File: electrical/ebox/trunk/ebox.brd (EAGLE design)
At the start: 127 x 101.6 mm, 159 parts, among them IC1 MAX3221CUE, IC10 SN74LVC1G125, IC11 MAX3221CUE, IC12 INA170, IC13 SN74LVC1G125, IC14 SN74LVC1G125, IC15 MAX3221CUE, IC16 MCP170333MB, IC17 SN74LVC1G125, IC18 SN74LVC1G125, IC19 74ALS04D, IC2 LT3652, IC3 XMEGA128A1, IC4 LT1161, IC5 SN74LVC1G125, IC6 SN74LVC1G125, IC7 MAX3221CUE, IC8 INA170, IC9 SN74LVC1G125, Q1 FDD4141TO252, U1 BLUETOOTH-RN42, U2 D2523T_, X1 7381-3PG-300, X10 DEANS-MALE, X11 B4B-ZR, X12 DEANS-MALE, X13 B4B-ZR, X14 22-23-2021, X15 DEANS-FEMALE, X16 DEANS-FEMALE, X17 USB_A, X2 7381-3PG-300, X3 7381-2PG-300, X4 17984-7PG-300, X5 17984-7PG-300, X6 17984-7PG-300, X7 17984-7PG-300, X8 22-23-2031, X9 22-23-2031

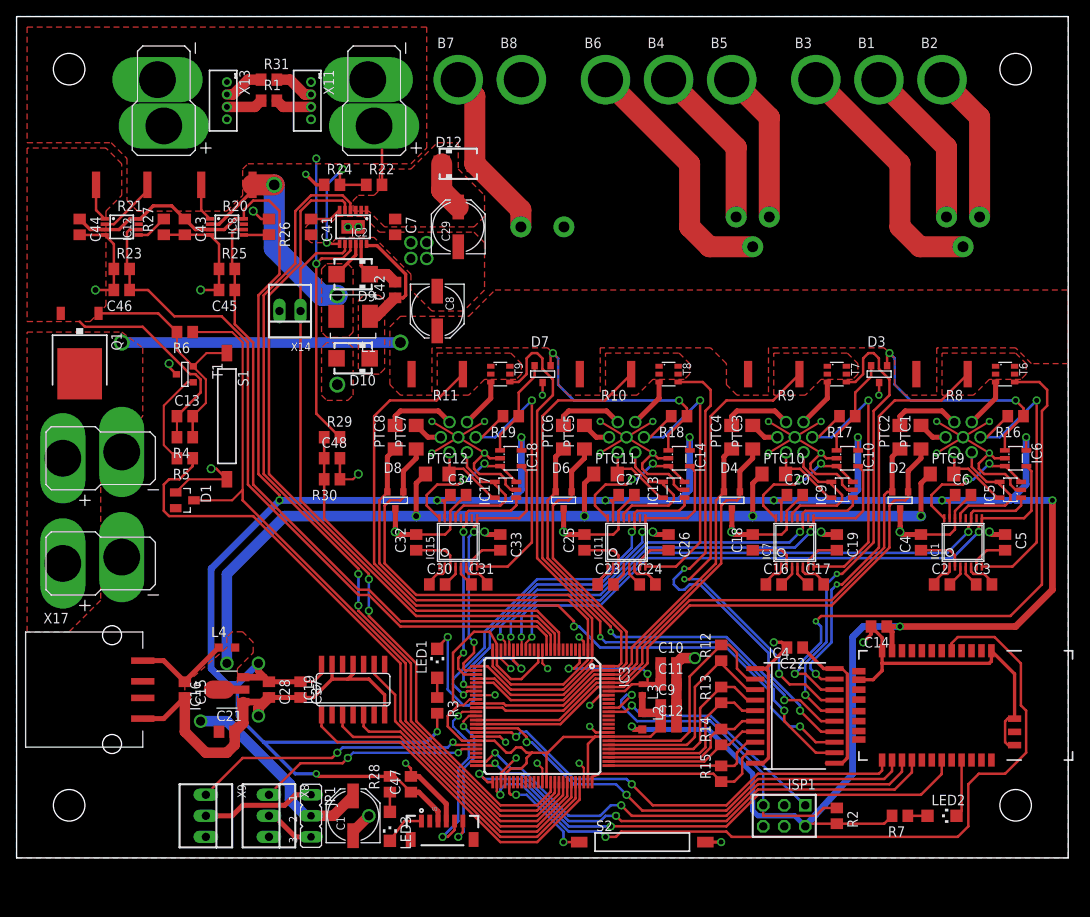
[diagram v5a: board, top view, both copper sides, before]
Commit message: Added water sensor connection.
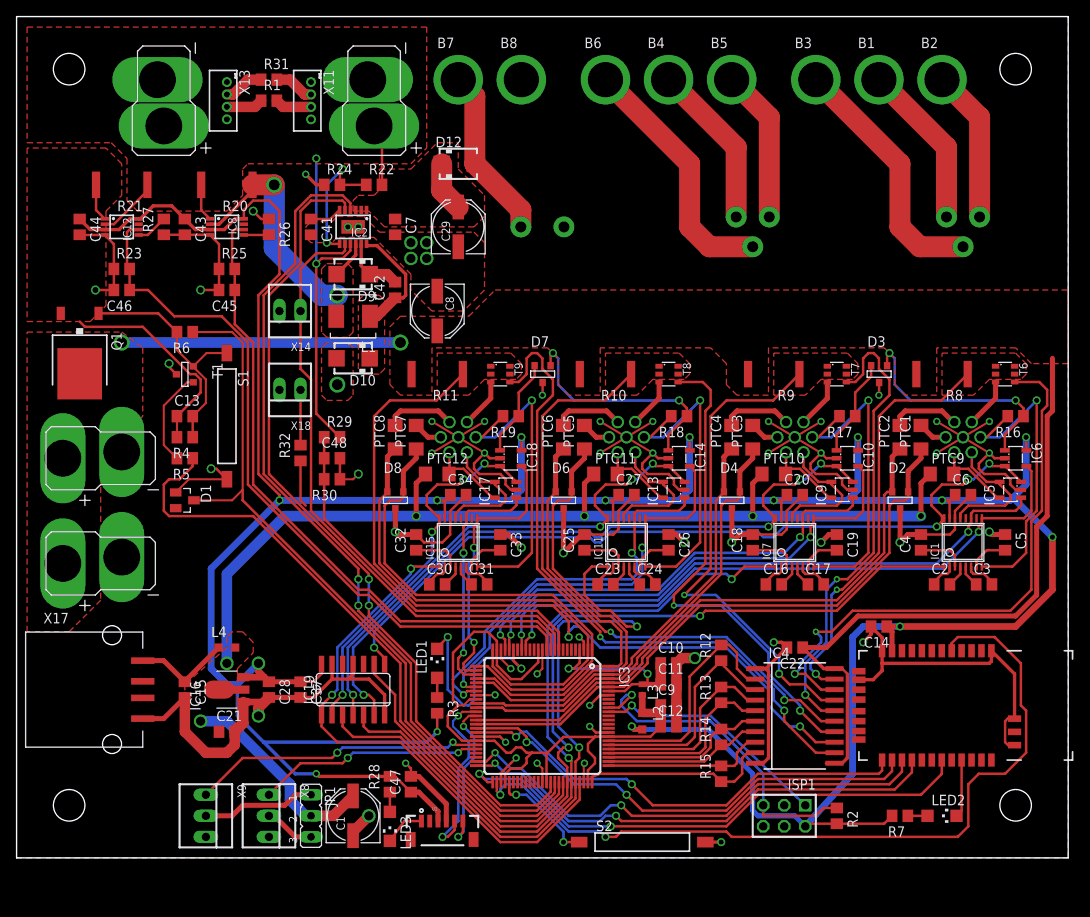
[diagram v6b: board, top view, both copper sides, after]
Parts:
- added R32: 1K, rcl:R0805
- added X18: 22-23-2021, con-molex:22-23-2021
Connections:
- new net N$17: IC3.8, R32.1
- new net WATER_SENSE: R32.2, X18.1
- net GND: now also X18.2
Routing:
- net EN232_1: track 16.8 -> 97.0 mm, vias 2 -> 4
- net !EN232_1: track 37.2 -> 108.4 mm, vias 0 -> 2
- net EN232_2: track 16.8 -> 84.6 mm, vias 2 -> 4
- net +12V: track 53.3 -> 113.6 mm
- net !EN232_2: track 35.3 -> 86.3 mm, vias 0 -> 2
- net EN232_3: track 16.8 -> 63.1 mm, vias 2 -> 4
- net !EN232_3: track 38.9 -> 82.6 mm, vias 0 -> 2
- net EN232_4: track 16.8 -> 45.9 mm, vias 2 -> 4
- net !EN232_4: track 42.6 -> 68.3 mm, vias 0 -> 2
- net GND: track 385.8 -> 395.5 mm
- net WATER_SENSE: track 0.00 -> 6.67 mm
- net N$17: track 0.00 -> 5.66 mm
- net TX3_TTL: track 45.1 -> 47.8 mm
- net +3V3: track 426.1 -> 423.5 mm
- net RX3_TTL: track 47.6 -> 49.8 mm
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
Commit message: Routed stuff up again.  Seem to have a ground plane partition to resolve.
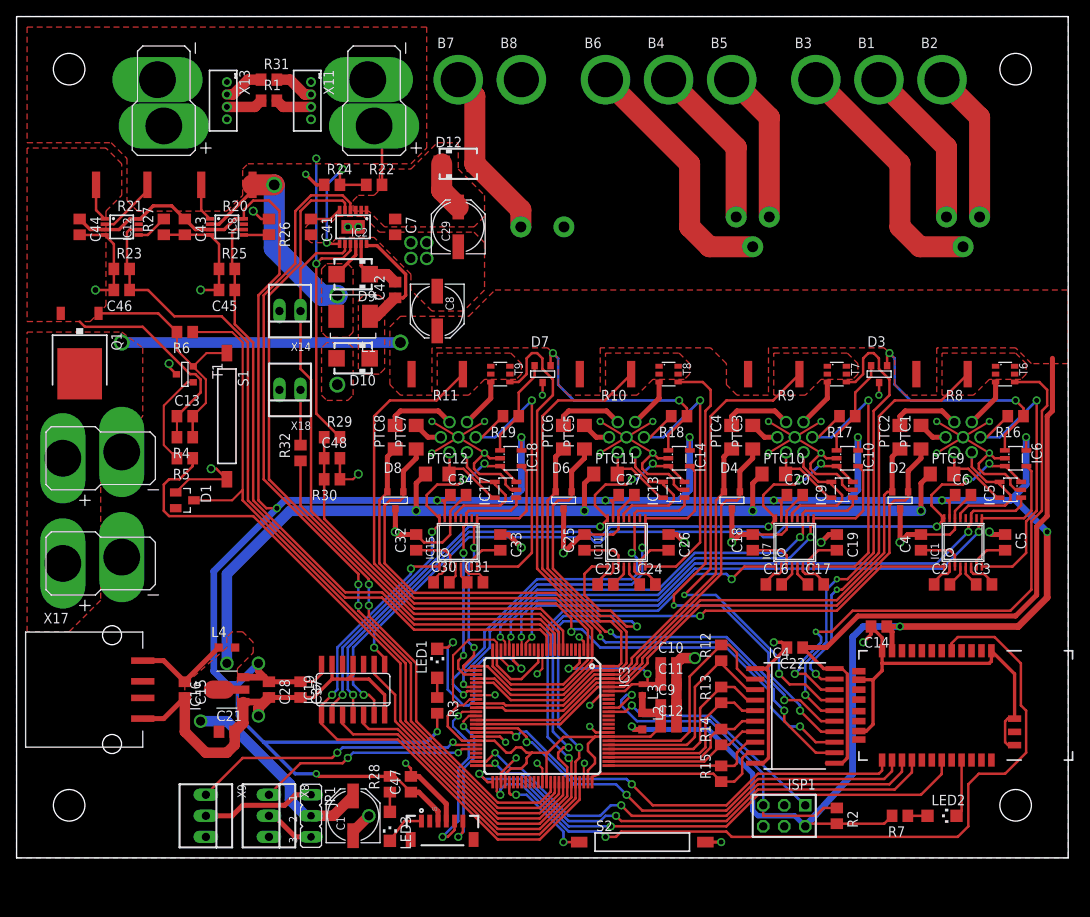
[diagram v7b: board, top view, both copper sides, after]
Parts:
- moved C30 0.57 mm to (51.3, 33.3)
- moved C31 0.57 mm to (55.4, 33.3)
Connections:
- net BATT_TEMP: now also IC3.9; no longer IC3.10
- net BATT_VSENSE: now also IC3.8; no longer IC3.9
- net N$17: now also IC3.10; no longer IC3.8
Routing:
- net N$17: track 5.66 -> 44.4 mm
- net GND: track 395.5 -> 402.9 mm
- net +5V: track 144.9 -> 142.7 mm
- net N$16: track 98.8 -> 97.5 mm
- net BATT_CURR_OUT: track 88.0 -> 89.1 mm
- net BATT_CURR_IN: track 78.3 -> 79.4 mm
- net AVR_VCC: track 81.9 -> 80.8 mm
- net N$34: track 3.31 -> 2.62 mm
- net BATT_VSENSE: track 46.0 -> 46.6 mm
- net +3V3: track 423.5 -> 424.1 mm
- net BATT_TEMP: track 74.4 -> 74.9 mm

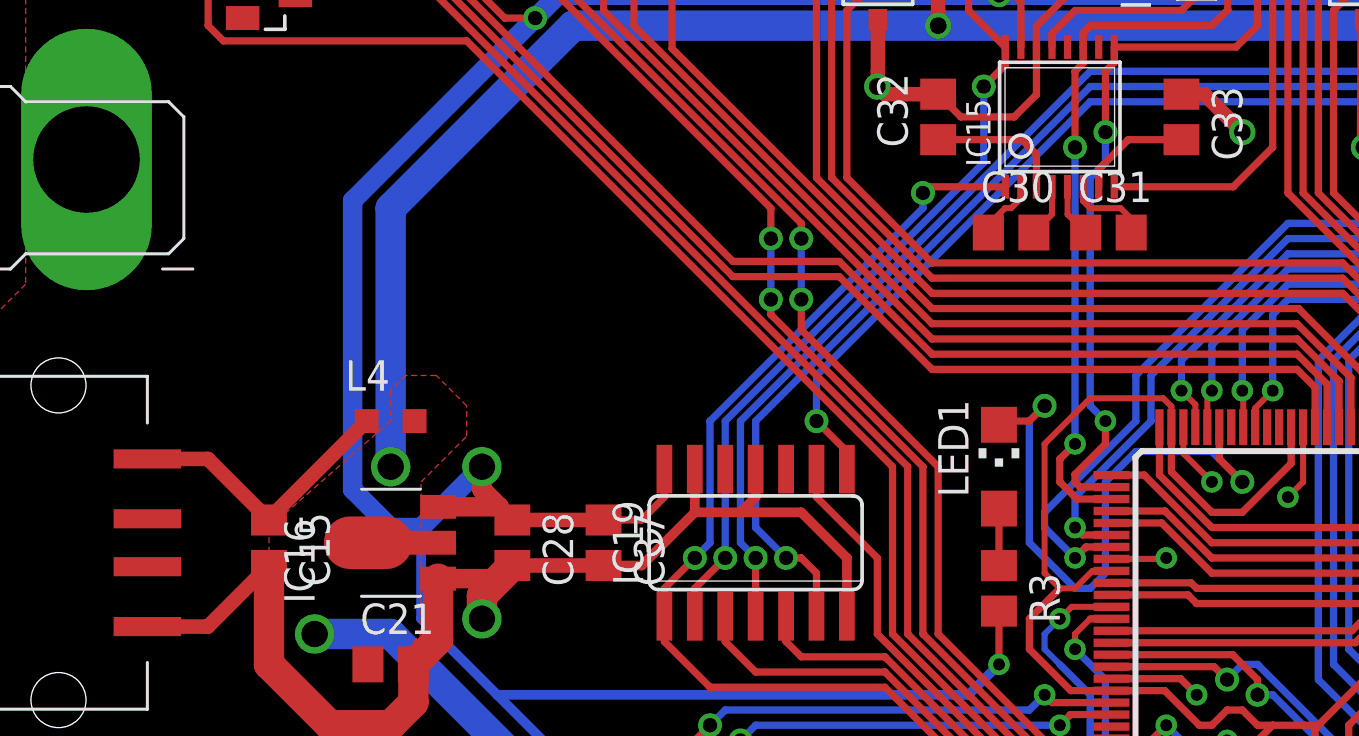
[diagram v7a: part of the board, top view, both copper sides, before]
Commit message: Fixed last few airwires, on to trace optimization for a bit.
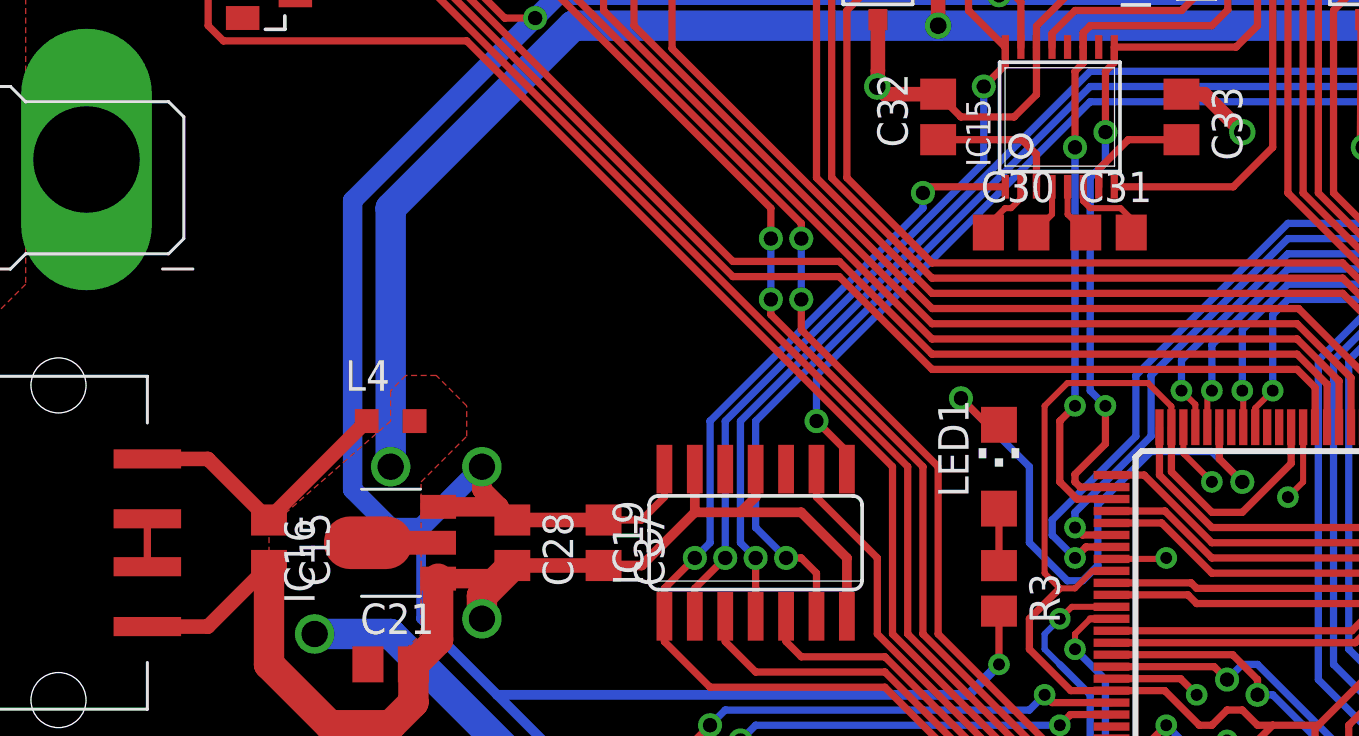
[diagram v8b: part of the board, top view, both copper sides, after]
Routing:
- net N$45: track 0.00 -> 2.00 mm
- net AVR_VCC: track 80.8 -> 82.2 mm
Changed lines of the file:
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@@
 <wire x1="102.6275" y1="15.315" x2="103.43" y2="16.1175" width="0.4064" layer="1"/>
 <wire x1="103.43" y1="21.515" x2="103.43" y2="16.1175" width="0.4064" layer="1"/>
-<wire x1="74.61" y1="43.815" x2="76.2" y2="46.355" width="0" layer="19" extent="1-1"/>
 </signal>
 <signal name="S1_12V">
@@
 <wire x1="55.5" y1="14.145" x2="53.8" y2="14.145" width="0.3048" layer="1"/>
 <wire x1="53.8" y1="14.145" x2="52.07" y2="15.875" width="0.3048" layer="1"/>
-<wire x1="52.705" y1="19.05" x2="52.705" y2="24.4475" width="0.254" layer="1"/>
-<wire x1="52.705" y1="24.4475" x2="54.61" y2="26.3525" width="0.254" layer="1"/>
-<wire x1="54.61" y1="26.3525" x2="57.658" y2="26.3525" width="0.254" layer="1"/>
+<wire x1="52.705" y1="19.05" x2="52.705" y2="26.035" width="0.254" layer="1"/>
+<wire x1="52.705" y1="26.035" x2="53.6575" y2="26.9875" width="0.254" layer="1"/>
+<wire x1="53.6575" y1="26.9875" x2="57.023" y2="26.9875" width="0.254" layer="1"/>
 <wire x1="64.135" y1="12.7" x2="66.04" y2="14.605" width="0.3048" layer="1"/>
 <wire x1="64" y1="9.145" x2="64" y2="12.565" width="0.3048" layer="1"/>
@@
 <wire x1="69" y1="9.145" x2="69" y2="10.58" width="0.3048" layer="1"/>
 <wire x1="58" y1="25.145" x2="58" y2="26.0105" width="0.254" layer="1"/>
-<wire x1="58" y1="26.0105" x2="57.658" y2="26.3525" width="0.254" layer="1"/>
+<wire x1="58" y1="26.0105" x2="57.023" y2="26.9875" width="0.254" layer="1"/>
 </signal>
 <signal name="AVR_AVCC">
@@
 <wire x1="54.285" y1="20.645" x2="53.975" y2="20.955" width="0.3048" layer="1"/>
 <via x="53.975" y="20.955" extent="1-16" drill="0.5"/>
-<wire x1="53.975" y1="20.955" x2="53.975" y2="22.225" width="0.3048" layer="16"/>
-<wire x1="53.975" y1="22.225" x2="57.15" y2="25.4" width="0.3048" layer="16"/>
+<wire x1="53.975" y1="20.955" x2="53.975" y2="21.59" width="0.3048" layer="16"/>
+<wire x1="53.975" y1="21.59" x2="57.15" y2="24.765" width="0.3048" layer="16"/>
 <via x="75.565" y="37.465" extent="1-16" drill="0.6"/>
 <wire x1="75.565" y1="37.465" x2="75.935" y2="37.835" width="0.3048" layer="1"/>
 <wire x1="75.935" y1="37.835" x2="75.935" y2="41.0178" width="0.3048" layer="1"/>
-<wire x1="57.15" y1="25.4" x2="57.15" y2="27.305" width="0.3048" layer="16"/>
+<wire x1="57.15" y1="24.765" x2="57.15" y2="27.305" width="0.3048" layer="16"/>
 <wire x1="57.15" y1="27.305" x2="62.865" y2="33.02" width="0.3048" layer="16"/>
 <wire x1="62.865" y1="33.02" x2="74.295" y2="33.02" width="0.3048" layer="16"/>
@@
 <wire x1="74.295" y1="36.83" x2="74.635" y2="37.17" width="0.3048" layer="1"/>
 <wire x1="74.635" y1="37.17" x2="74.635" y2="41.0178" width="0.3048" layer="1"/>
-<wire x1="53.975" y1="19.685" x2="52.705" y2="20.955" width="0.3048" layer="16"/>
-<wire x1="52.705" y1="20.955" x2="52.705" y2="21.59" width="0.3048" layer="16"/>
-<wire x1="52.705" y1="21.59" x2="56.515" y2="25.4" width="0.3048" layer="16"/>
-<wire x1="56.515" y1="25.4" x2="56.515" y2="27.305" width="0.3048" layer="16"/>
+<wire x1="53.0225" y1="21.2725" x2="56.515" y2="24.765" width="0.3048" layer="16"/>
+<wire x1="56.515" y1="24.765" x2="56.515" y2="27.305" width="0.3048" layer="16"/>
 <wire x1="56.515" y1="27.305" x2="62.865" y2="33.655" width="0.3048" layer="16"/>
 <wire x1="74.295" y1="33.655" x2="62.865" y2="33.655" width="0.3048" layer="16"/>
@@
 <wire x1="74.93" y1="34.29" x2="74.93" y2="36.195" width="0.3048" layer="16"/>
 <wire x1="74.93" y1="36.195" x2="74.295" y2="36.83" width="0.3048" layer="16"/>
+<wire x1="53.0225" y1="21.2725" x2="53.0225" y2="20.6375" width="0.3048" layer="16"/>
+<wire x1="53.0225" y1="20.6375" x2="53.975" y2="19.685" width="0.3048" layer="16"/>
 </signal>
 <signal name="RX4_TTL">
@@
 <wire x1="54.19" y1="22.645" x2="53.975" y2="22.86" width="0.3048" layer="1"/>
 <wire x1="53.975" y1="22.86" x2="53.975" y2="23.1775" width="0.3048" layer="1"/>
-<via x="55.245" y="25.4" extent="1-16" drill="0.5"/>
-<wire x1="55.245" y1="25.4" x2="54.61" y2="26.035" width="0.3048" layer="16"/>
-<wire x1="54.61" y1="26.035" x2="54.61" y2="35.56" width="0.3048" layer="16"/>
+<via x="55.245" y="26.035" extent="1-16" drill="0.5"/>
+<wire x1="55.245" y1="26.035" x2="54.61" y2="26.67" width="0.3048" layer="16"/>
+<wire x1="54.61" y1="26.67" x2="54.61" y2="35.56" width="0.3048" layer="16"/>
 <via x="55.245" y="37.465" extent="1-16" drill="0.6"/>
 <wire x1="55.245" y1="37.465" x2="55.245" y2="40.005" width="0.3048" layer="1"/>
@@
 <wire x1="55.615" y1="40.375" x2="55.245" y2="40.005" width="0.3048" layer="1"/>
 <wire x1="53.975" y1="23.1775" x2="55.245" y2="24.4475" width="0.3048" layer="1"/>
-<wire x1="55.245" y1="24.4475" x2="55.245" y2="25.4" width="0.3048" layer="1"/>
+<wire x1="55.245" y1="24.4475" x2="55.245" y2="26.035" width="0.3048" layer="1"/>
 <wire x1="54.61" y1="35.56" x2="55.245" y2="36.195" width="0.3048" layer="16"/>
 <wire x1="55.245" y1="36.195" x2="55.245" y2="37.465" width="0.3048" layer="16"/>
@@
 <wire x1="55.5" y1="22.145" x2="54.055" y2="22.145" width="0.3048" layer="1"/>
 <wire x1="54.055" y1="22.145" x2="53.34" y2="22.86" width="0.3048" layer="1"/>
-<wire x1="53.34" y1="22.86" x2="53.34" y2="23.8125" width="0.3048" layer="1"/>
-<wire x1="53.34" y1="23.8125" x2="53.975" y2="24.4475" width="0.3048" layer="1"/>
-<via x="53.975" y="24.4475" extent="1-16" drill="0.5"/>
-<wire x1="53.975" y1="24.4475" x2="53.975" y2="36.83" width="0.3048" layer="16"/>
+<wire x1="53.34" y1="22.86" x2="53.34" y2="25.4" width="0.3048" layer="1"/>
+<wire x1="53.34" y1="25.4" x2="53.975" y2="26.035" width="0.3048" layer="1"/>
+<via x="53.975" y="26.035" extent="1-16" drill="0.5"/>
+<wire x1="53.975" y1="26.035" x2="53.975" y2="36.83" width="0.3048" layer="16"/>
 <via x="53.975" y="36.83" extent="1-16" drill="0.6"/>
 <wire x1="53.975" y1="36.83" x2="53.975" y2="40.005" width="0.3048" layer="1"/>
@@
 <via x="60.96" y="22.86" extent="1-16" drill="0.6"/>
 <wire x1="60.96" y1="22.86" x2="59.69" y2="24.13" width="0.3048" layer="16"/>
-<wire x1="59.69" y1="24.13" x2="56.515" y2="24.13" width="0.3048" layer="16"/>
-<wire x1="56.515" y1="24.13" x2="55.245" y2="22.86" width="0.3048" layer="16"/>
-<wire x1="55.245" y1="22.86" x2="55.245" y2="19.05" width="0.3048" layer="16"/>
-<wire x1="55.245" y1="19.05" x2="54.61" y2="18.415" width="0.3048" layer="16"/>
-<wire x1="54.61" y1="18.415" x2="53.975" y2="18.415" width="0.3048" layer="16"/>
-<wire x1="53.975" y1="18.415" x2="52.07" y2="20.32" width="0.3048" layer="16"/>
-<via x="52.705" y="26.035" extent="1-16" drill="0.6"/>
+<wire x1="59.69" y1="24.13" x2="57.15" y2="24.13" width="0.3048" layer="16"/>
+<wire x1="57.15" y1="24.13" x2="54.9275" y2="21.9075" width="0.3048" layer="16"/>
+<wire x1="54.9275" y1="21.9075" x2="54.9275" y2="19.3675" width="0.3048" layer="16"/>
+<wire x1="54.9275" y1="19.3675" x2="54.2925" y2="18.7325" width="0.3048" layer="16"/>
+<wire x1="54.2925" y1="18.7325" x2="53.6575" y2="18.7325" width="0.3048" layer="16"/>
+<wire x1="53.6575" y1="18.7325" x2="52.07" y2="20.32" width="0.3048" layer="16"/>
+<via x="49.2125" y="26.3525" extent="1-16" drill="0.6"/>
 <wire x1="50.8" y1="25.245" x2="50.8" y2="25.4" width="0.3048" layer="1"/>
-<wire x1="52.07" y1="20.32" x2="52.07" y2="25.4" width="0.3048" layer="16"/>
-<wire x1="52.07" y1="25.4" x2="52.705" y2="26.035" width="0.3048" layer="16"/>
-<wire x1="50.8" y1="25.4" x2="52.07" y2="25.4" width="0.3048" layer="1"/>
-<wire x1="52.07" y1="25.4" x2="52.705" y2="26.035" width="0.3048" layer="1"/>
+<wire x1="52.07" y1="20.32" x2="52.07" y2="23.495" width="0.3048" layer="16"/>
+<wire x1="52.07" y1="23.495" x2="49.2125" y2="26.3525" width="0.3048" layer="16"/>
+<wire x1="50.8" y1="25.4" x2="50.165" y2="25.4" width="0.3048" layer="1"/>
+<wire x1="50.165" y1="25.4" x2="49.2125" y2="26.3525" width="0.3048" layer="1"/>
 </signal>
 <signal name="N$6">
@@
 <contactref element="X17" pad="2"/>
 <contactref element="X17" pad="3"/>
-<wire x1="15.24" y1="19.32" x2="15.24" y2="21.32" width="0" layer="19" extent="1-1"/>
+<wire x1="15.24" y1="21.32" x2="15.24" y2="19.32" width="0.3048" layer="1"/>
 </signal>
 <signal name="N$46">
